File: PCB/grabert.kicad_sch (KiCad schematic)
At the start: 14 parts, among them J1 Conn_01x02, J2 Conn_01x02, J3 Conn_01x05, J4 USB_C_Receptacle_USB2.0, J5 SSD1306, SW1 RotaryEncoder_Switch, U1 AMS1117-3.3, U2 STM32F072V8Tx

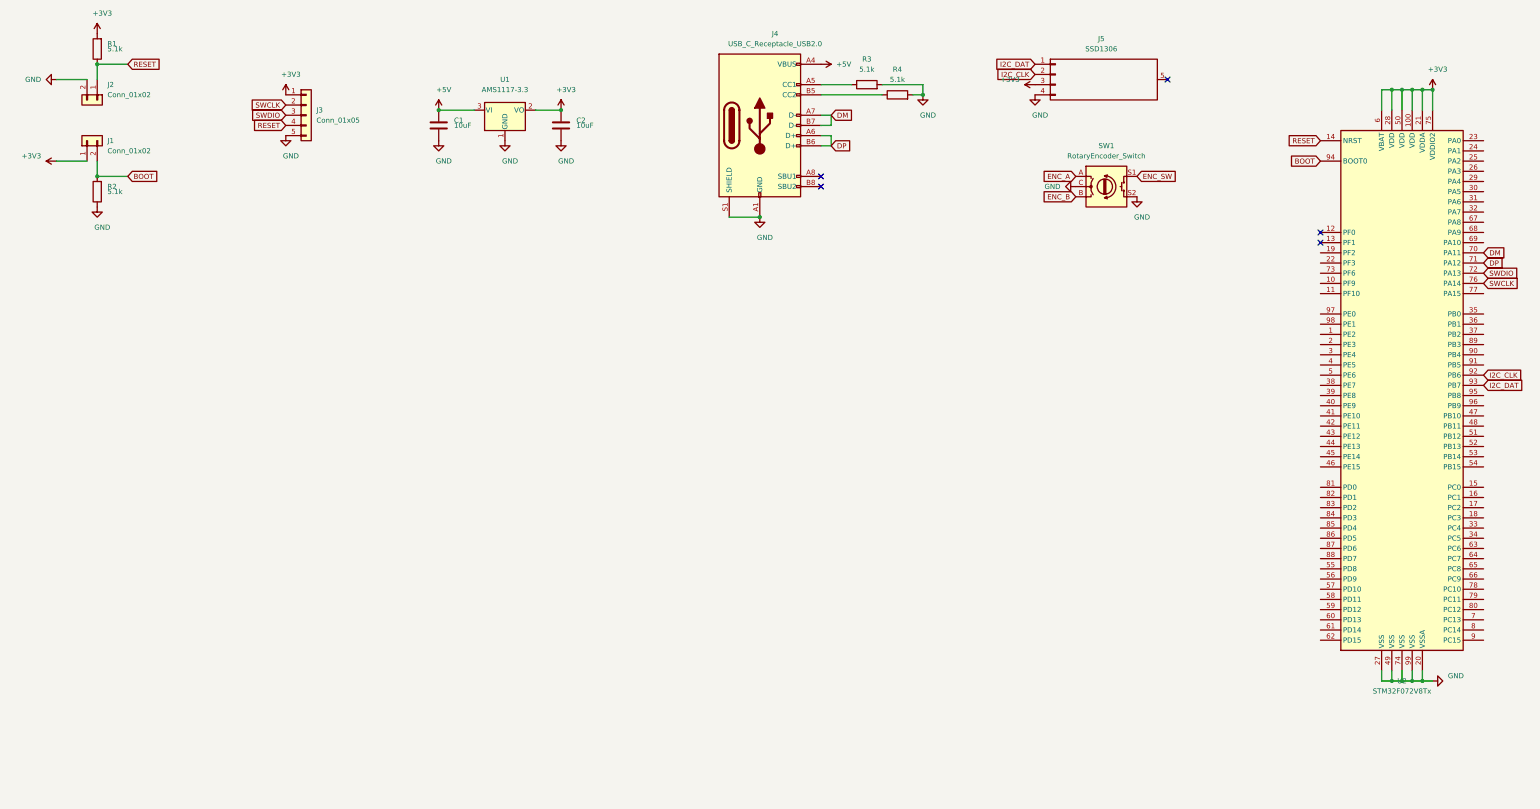
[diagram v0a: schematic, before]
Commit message: switches added
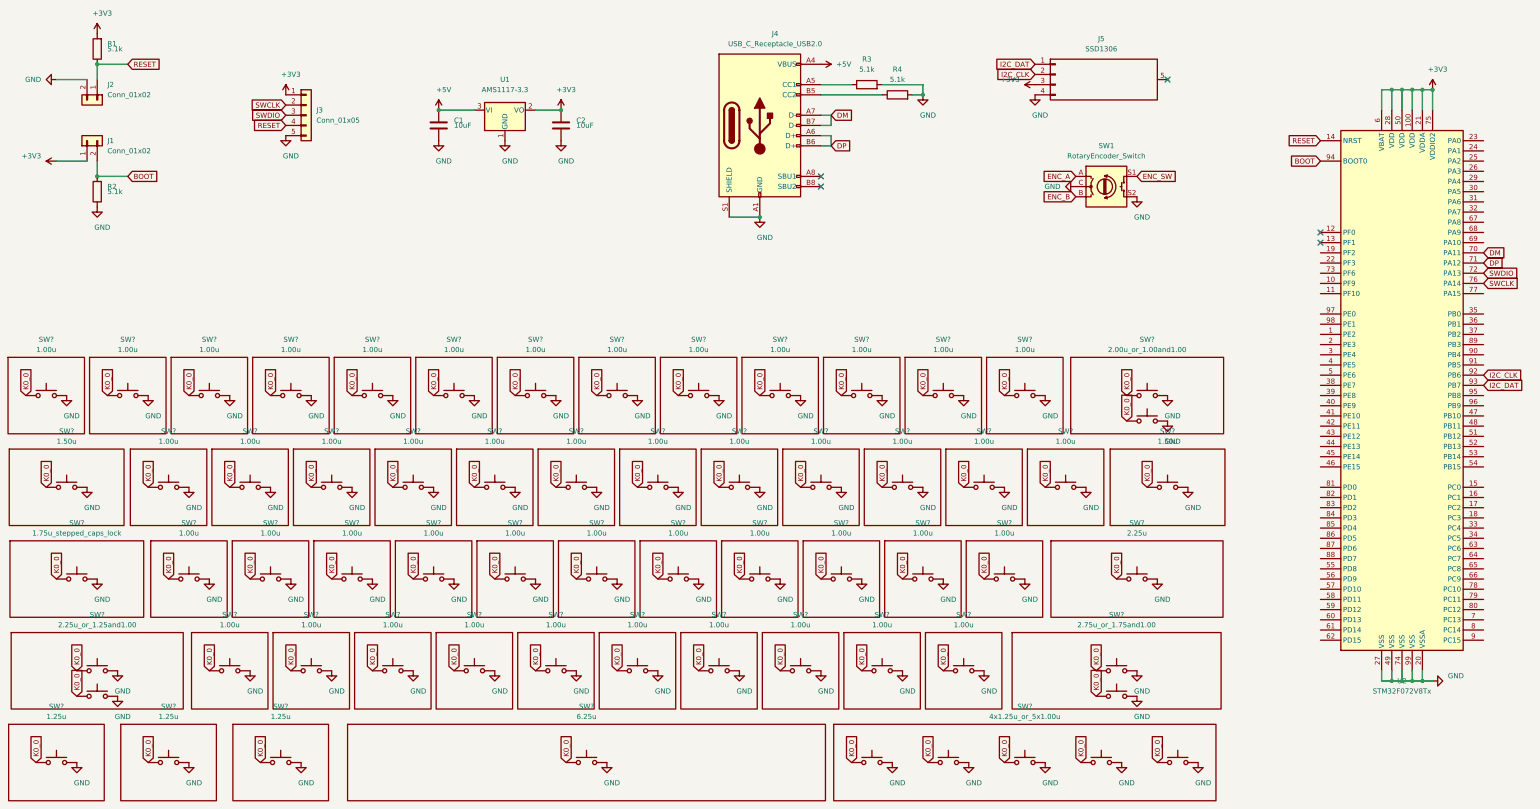
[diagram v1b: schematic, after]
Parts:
- added SW? (x46): 1.00u, kobuss-footprint:MX_1u, symbol kobuss:1.00u
- added SW? (x2): 1.50u, kobuss-footprint:MX_1.50u, symbol kobuss:1.50u
- added SW?: 1.75u_stepped_caps_lock, kobuss-footprint:MX_1.75u_stepped_caps, symbol kobuss:1.75u_stepped_caps_lock
- added SW? (x3): 1.25u, kobuss-footprint:MX_1.25, symbol kobuss:1.25u
- added SW?: 2.75u_or_1.75and1.00, kobuss-footprint:MX_2.75u_or_1.75and1.00, symbol kobuss:2.75u_or_1.75and1.00
- added SW?: 2.25u_or_1.25and1.00, kobuss-footprint:MX_2.25u_or_1.25and1.00, symbol kobuss:2.25u_or_1.25and1.00
- added SW?: 2.00u_or_1.00and1.00, kobuss-footprint:MX_2.00u_or_1.00and1.00, symbol kobuss:2.00u_or_1.00and1.00
- added SW?: 2.25u, kobuss-footprint:MX_2.25u, symbol kobuss:2.25u
- added SW?: 6.25u, kobuss-footprint:MX_6.25u, symbol kobuss:6.25u
- added SW?: 4x1.25u_or_5x1.00u, kobuss-footprint:MX_4x1.25u_or_5x1.00u, symbol kobuss:4x1.25u_or_5x1.00u
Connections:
- net GND: now also SW?.10, SW?.2, SW?.2, SW?.2, SW?.2, SW?.2, SW?.2, SW?.2, SW?.2, SW?.2, SW?.2, SW?.2, SW?.2, SW?.2, SW?.2, SW?.2, SW?.2, SW?.2, SW?.2, SW?.2, SW?.2, SW?.2, SW?.2, SW?.2, SW?.2, SW?.2, SW?.2, SW?.2, SW?.2, SW?.2, SW?.2, SW?.2, SW?.2, SW?.2, SW?.2, SW?.2, SW?.2, SW?.2, SW?.2, SW?.2, SW?.2, SW?.2, SW?.2, SW?.2, SW?.2, SW?.2, SW?.2, SW?.2, SW?.2, SW?.2, SW?.2, SW?.2, SW?.2, SW?.2, SW?.2, SW?.2, SW?.2, SW?.2, SW?.2, SW?.4, SW?.4, SW?.4, SW?.4, SW?.6, SW?.8
- new net K0_0: SW?.1, SW?.1, SW?.1, SW?.1, SW?.1, SW?.1, SW?.1, SW?.1, SW?.1, SW?.1, SW?.1, SW?.1, SW?.1, SW?.1, SW?.1, SW?.1, SW?.1, SW?.1, SW?.1, SW?.1, SW?.1, SW?.1, SW?.1, SW?.1, SW?.1, SW?.1, SW?.1, SW?.1, SW?.1, SW?.1, SW?.1, SW?.1, SW?.1, SW?.1, SW?.1, SW?.1, SW?.1, SW?.1, SW?.1, SW?.1, SW?.1, SW?.1, SW?.1, SW?.1, SW?.1, SW?.1, SW?.1, SW?.1, SW?.1, SW?.1, SW?.1, SW?.1, SW?.1, SW?.1, SW?.1, SW?.1, SW?.1, SW?.1, SW?.3, SW?.3, SW?.3, SW?.3, SW?.5, SW?.7, SW?.9

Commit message: switches placed
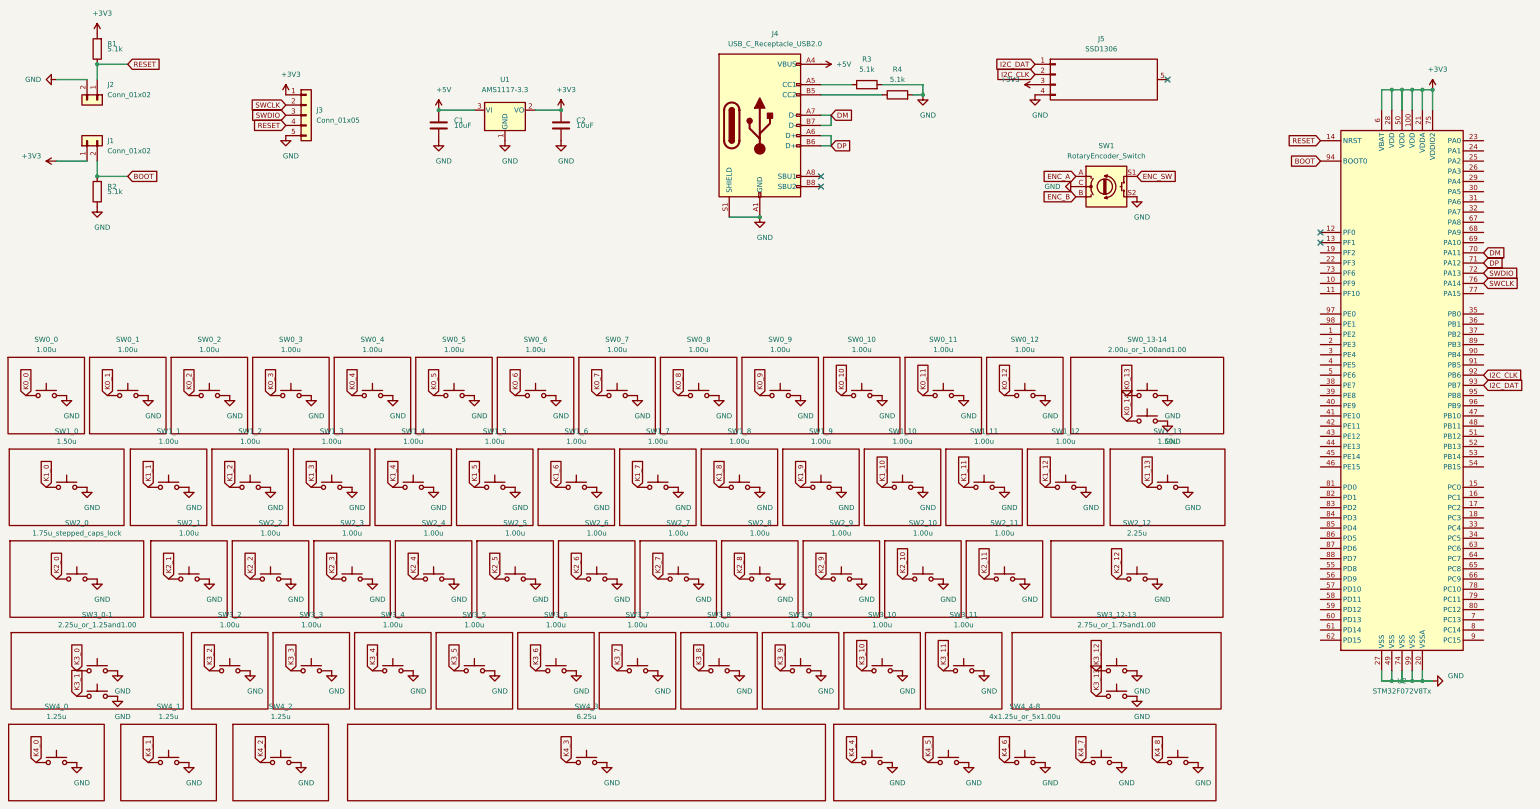
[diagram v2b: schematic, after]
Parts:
- gave numbers to parts that had none: 58
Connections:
- net K0_0: no longer SW0_1.1, SW0_10.1, SW0_11.1, SW0_12.1, SW0_13-14.1, SW0_13-14.3, SW0_2.1, SW0_3.1, SW0_4.1, SW0_5.1, SW0_6.1, SW0_7.1, SW0_8.1, SW0_9.1, SW1_0.1, SW1_1.1, SW1_10.1, SW1_11.1, SW1_12.1, SW1_13.1, SW1_2.1, SW1_3.1, SW1_4.1, SW1_5.1, SW1_6.1, SW1_7.1, SW1_8.1, SW1_9.1, SW2_0.1, SW2_1.1, SW2_10.1, SW2_11.1, SW2_12.1, SW2_2.1, SW2_3.1, SW2_4.1, SW2_5.1, SW2_6.1, SW2_7.1, SW2_8.1, SW2_9.1, SW3_0-1.1, SW3_0-1.3, SW3_10.1, SW3_11.1, SW3_12-13.1, SW3_12-13.3, SW3_2.1, SW3_3.1, SW3_4.1, SW3_5.1, SW3_6.1, SW3_7.1, SW3_8.1, SW3_9.1, SW4_0.1, SW4_1.1, SW4_2.1, SW4_3.1, SW4_4-8.1, SW4_4-8.3, SW4_4-8.5, SW4_4-8.7, SW4_4-8.9
- new net K0_1: SW0_1.1
- new net K0_10: SW0_10.1
- new net K0_11: SW0_11.1
- new net K0_12: SW0_12.1
- new net K0_13: SW0_13-14.1
- new net K0_14: SW0_13-14.3
- new net K0_2: SW0_2.1
- new net K0_3: SW0_3.1
- new net K0_4: SW0_4.1
- new net K0_5: SW0_5.1
- new net K0_6: SW0_6.1
- new net K0_7: SW0_7.1
- new net K0_8: SW0_8.1
- new net K0_9: SW0_9.1
- new net K1_0: SW1_0.1
- new net K1_1: SW1_1.1
- new net K1_10: SW1_10.1
- new net K1_11: SW1_11.1
- new net K1_12: SW1_12.1
- new net K1_13: SW1_13.1
- new net K1_2: SW1_2.1
- new net K1_3: SW1_3.1
- new net K1_4: SW1_4.1
- new net K1_5: SW1_5.1
- new net K1_6: SW1_6.1
- new net K1_7: SW1_7.1
- new net K1_8: SW1_8.1
- new net K1_9: SW1_9.1
- new net K2_0: SW2_0.1
- new net K2_1: SW2_1.1
- new net K2_10: SW2_10.1
- new net K2_11: SW2_11.1
- new net K2_12: SW2_12.1
- new net K2_2: SW2_2.1
- new net K2_3: SW2_3.1
- new net K2_4: SW2_4.1
- new net K2_5: SW2_5.1
- new net K2_6: SW2_6.1
- new net K2_7: SW2_7.1
- new net K2_8: SW2_8.1
- new net K2_9: SW2_9.1
- new net K3_0: SW3_0-1.1
- new net K3_1: SW3_0-1.3
- new net K3_10: SW3_10.1
- new net K3_11: SW3_11.1
- new net K3_12: SW3_12-13.1
- new net K3_13: SW3_12-13.3
- new net K3_2: SW3_2.1
- new net K3_3: SW3_3.1
- new net K3_4: SW3_4.1
- new net K3_5: SW3_5.1
- new net K3_6: SW3_6.1
- new net K3_7: SW3_7.1
- new net K3_8: SW3_8.1
- new net K3_9: SW3_9.1
- new net K4_0: SW4_0.1
- new net K4_1: SW4_1.1
- new net K4_2: SW4_2.1
- new net K4_3: SW4_3.1
- new net K4_4: SW4_4-8.1
- new net K4_5: SW4_4-8.3
- new net K4_6: SW4_4-8.5
- new net K4_7: SW4_4-8.7
- new net K4_8: SW4_4-8.9
